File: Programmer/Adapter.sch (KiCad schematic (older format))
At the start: 5 parts, among them IC1 ARDUINO_PRO_MINI_BASIC, P1 CONN_01X06, P2 CONN_01X02, SW1 SWITCH_SPDT, SW2 SWITCH_SPDT

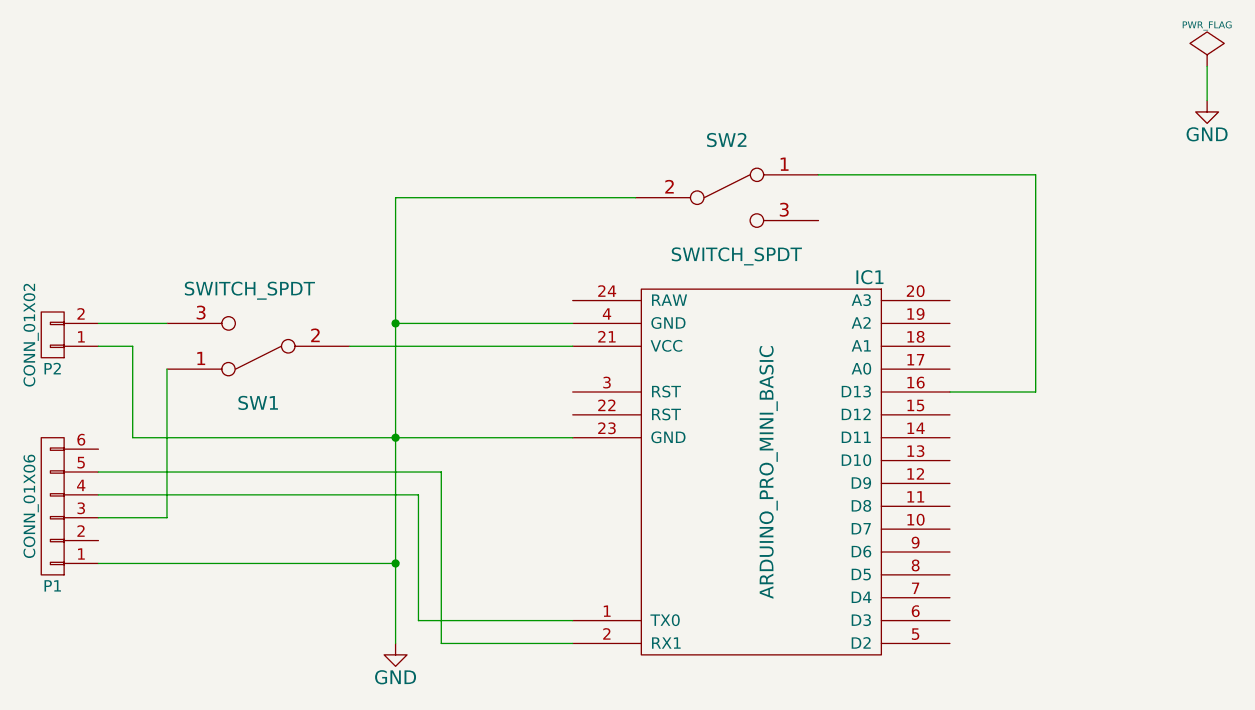
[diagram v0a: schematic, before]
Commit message: Use a different pin for bringing GPIO0 out
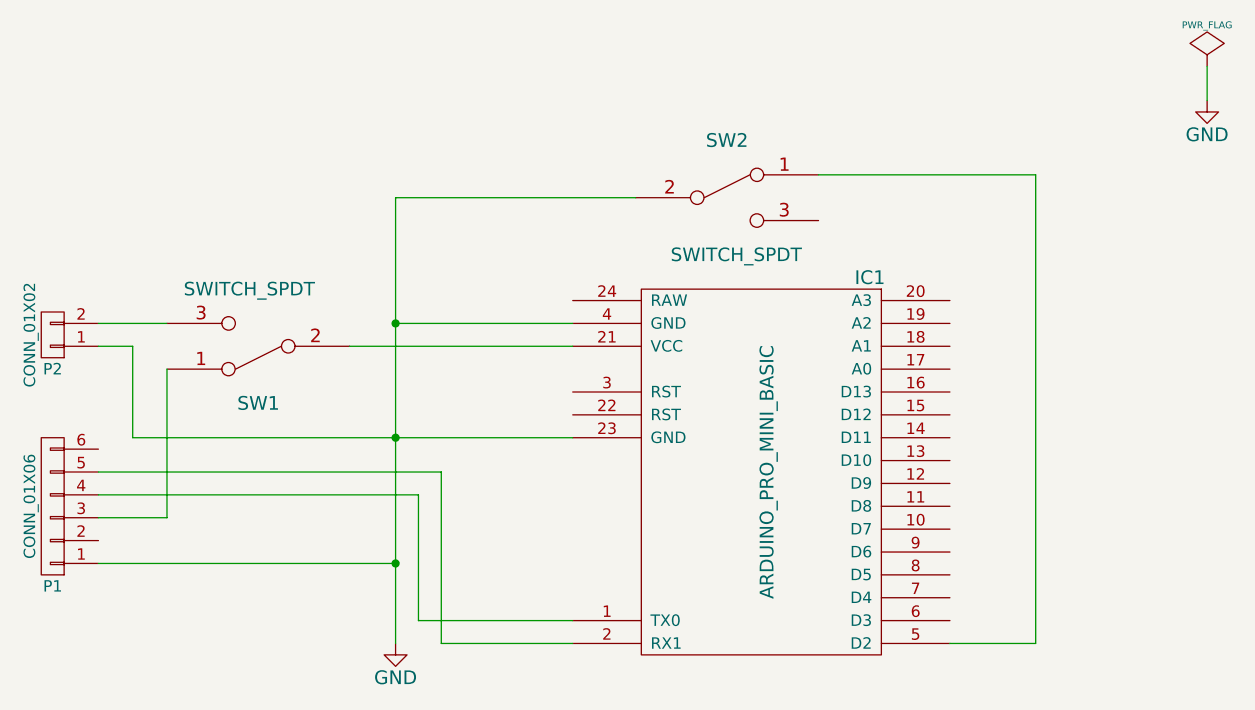
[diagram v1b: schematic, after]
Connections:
- net at IC1.16 (D13): no longer SW2.1
- net at IC1.5 (D2): now also SW2.1
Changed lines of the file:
@@
 	4900 4250 5475 4250
 Wire Wire Line
-	7500 3150 7125 3150
-Wire Wire Line
-	7500 2200 7500 3150
+	7500 2200 7500 4250
 $Comp
 L GND #PWR01
@@
 Wire Wire Line
 	3550 2950 3550 3350
+Wire Wire Line
+	7500 4250 7125 4250
 $EndSCHEMATC
